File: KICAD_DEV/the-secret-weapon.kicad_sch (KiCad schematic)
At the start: 0 parts

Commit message: ground pour + core SoC STM32H757
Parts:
- added U1: STM32H7A3IGTx, Package_QFP:LQFP-176_24x24mm_P0.5mm, symbol MCU_ST_STM32H7:STM32H7A3IGTx
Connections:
- new net GND: U1.102 (VSS), U1.113 (VSS), U1.126 (VSS), U1.135 (VSS), U1.14 (VSS), U1.148 (VSS), U1.158 (VSS), U1.22 (VSS), U1.37 (VSSA), U1.48 (VSS), U1.61 (VSS), U1.71 (VSS), U1.90 (VSS)

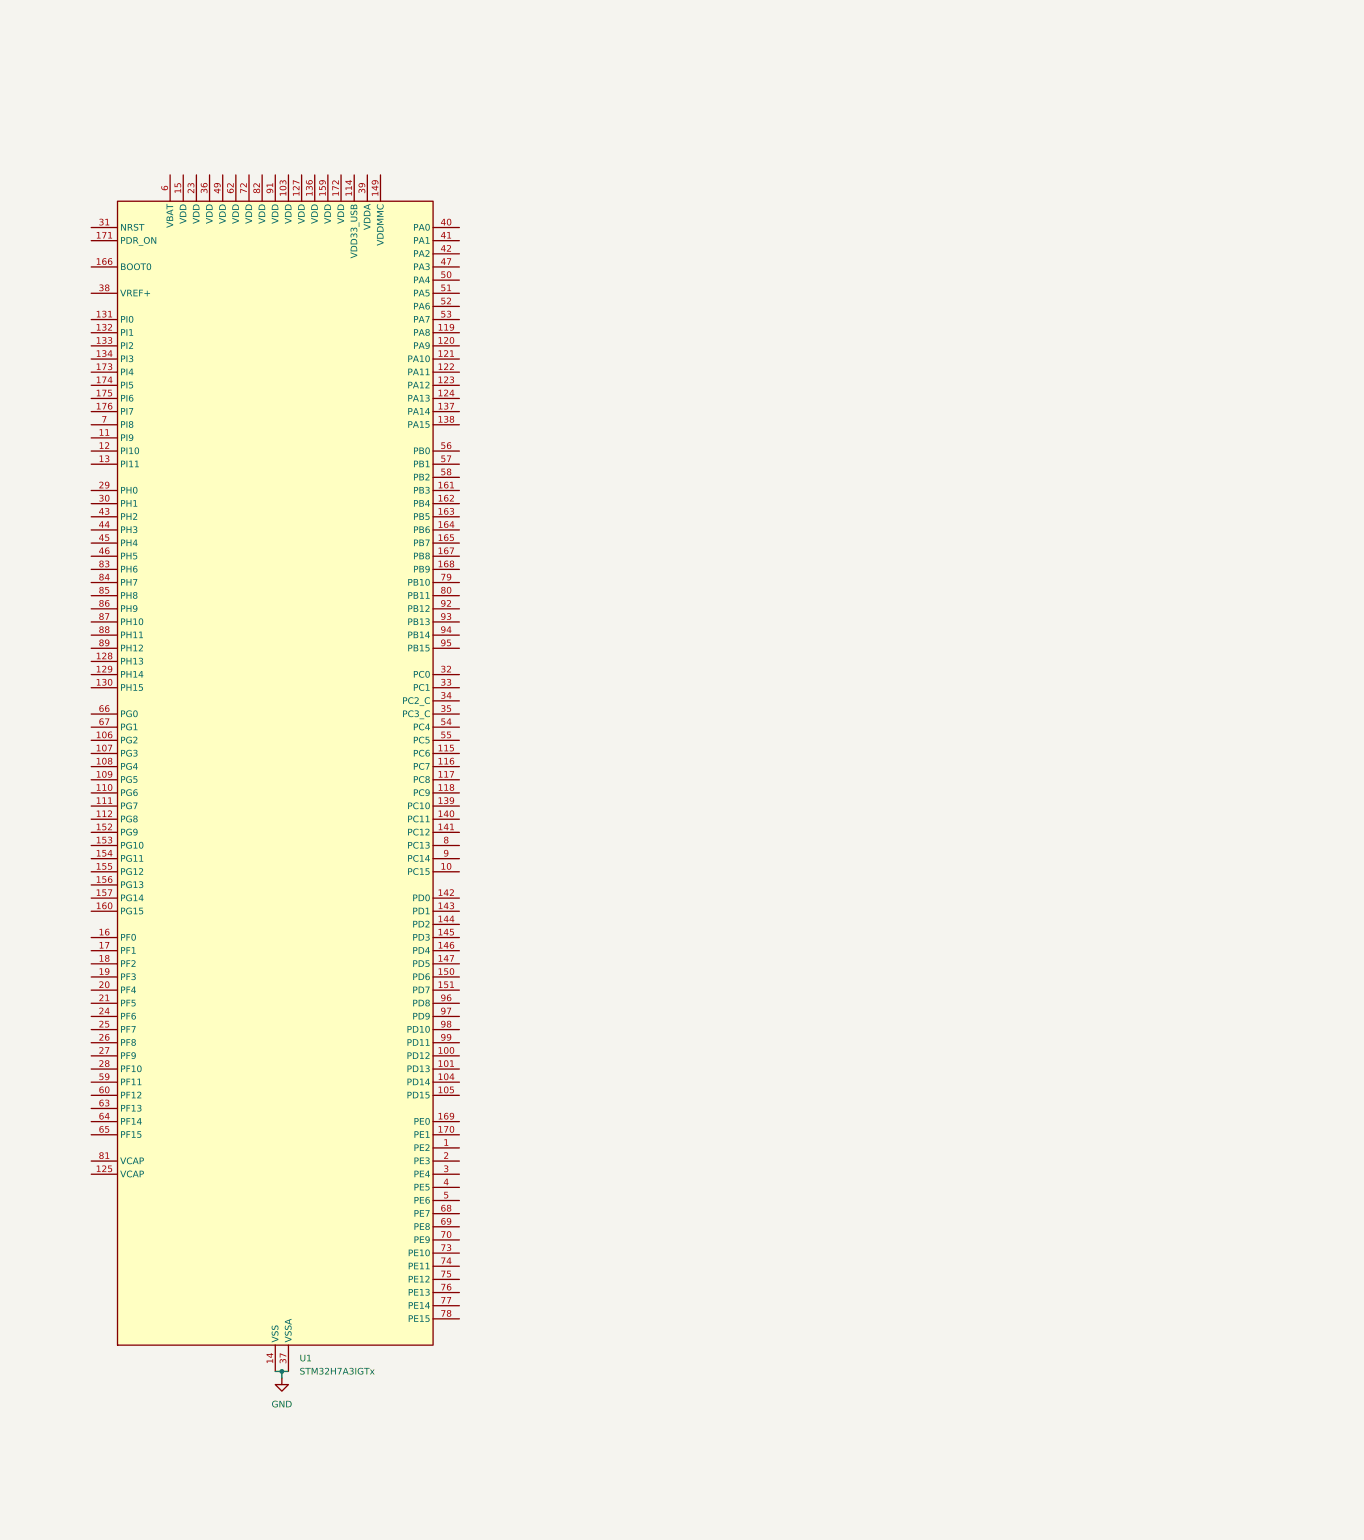
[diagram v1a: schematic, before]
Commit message: accidently used the wrong symbol
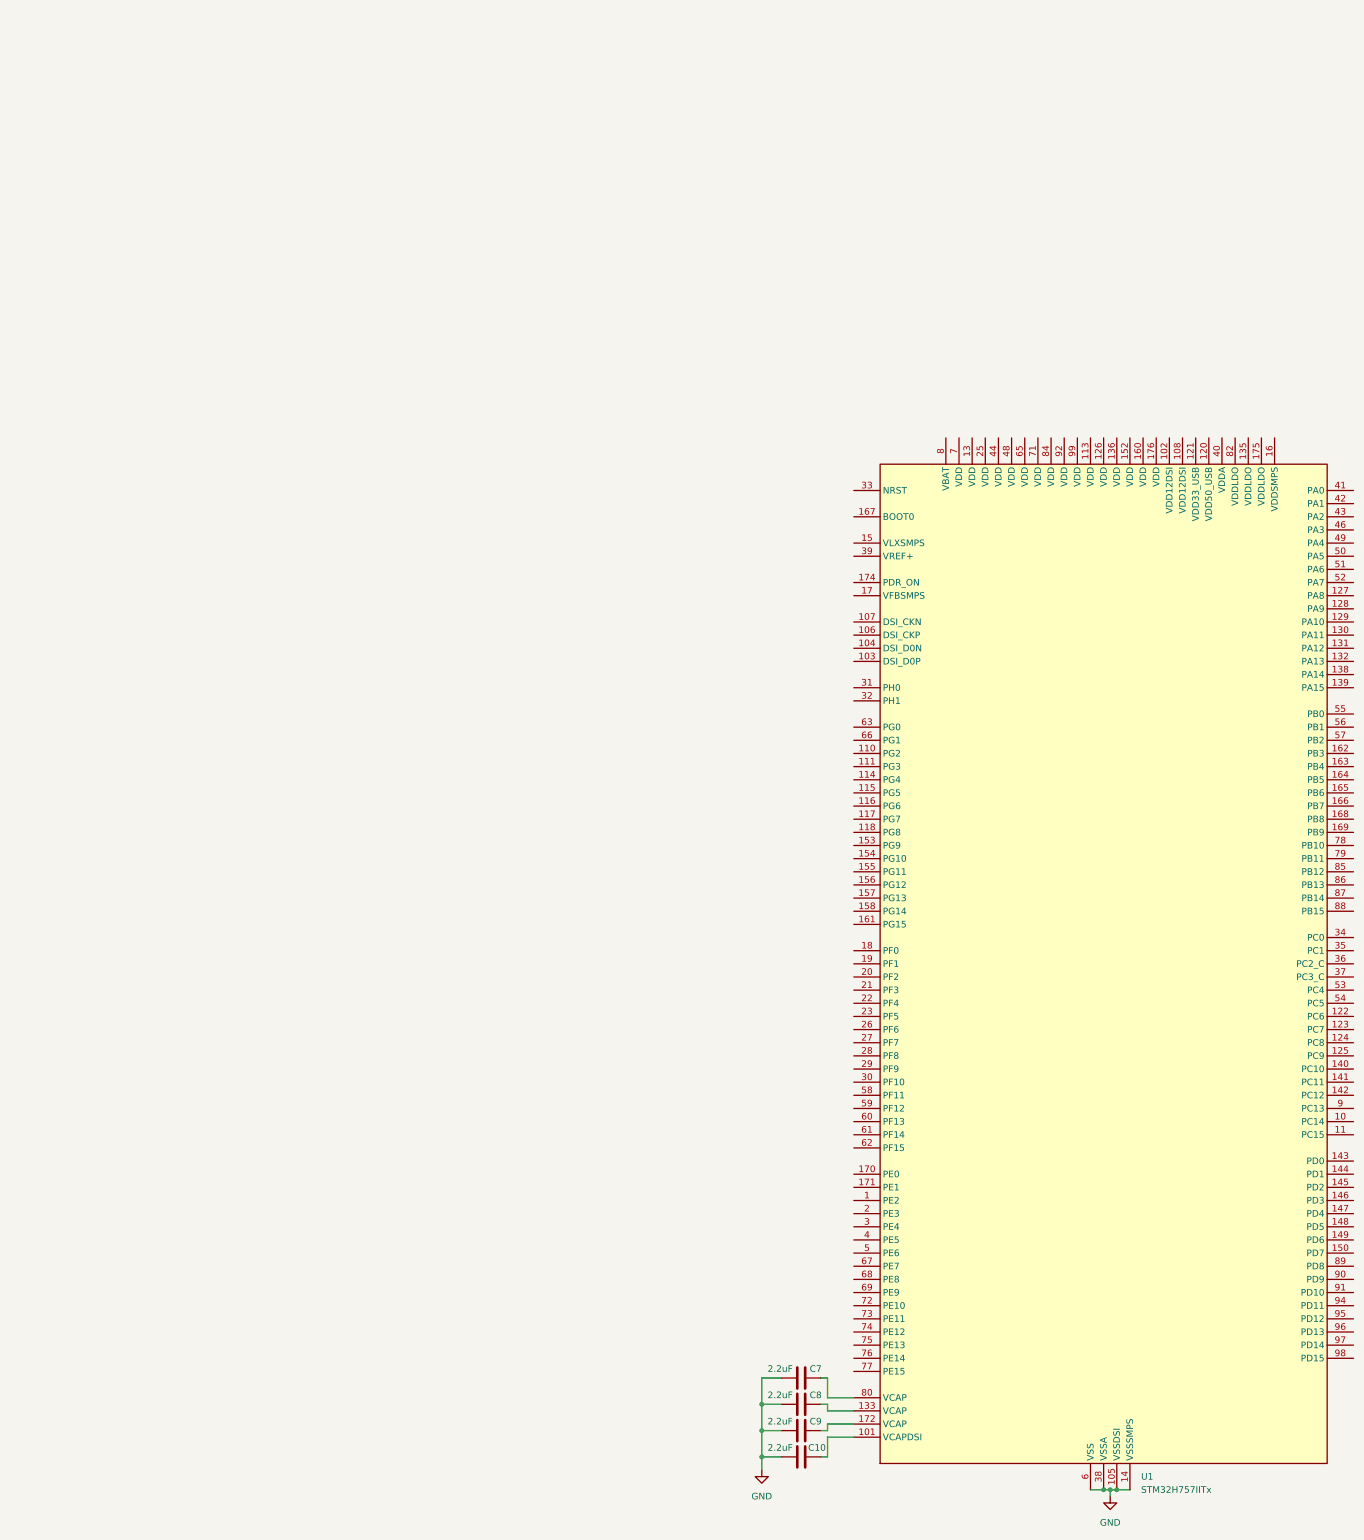
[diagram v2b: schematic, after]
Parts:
- removed U1: STM32H7A3IGTx, Package_QFP:LQFP-176_24x24mm_P0.5mm, symbol MCU_ST_STM32H7:STM32H7A3IGTx
- added C10, C7, C8, C9: 2.2uF, symbol Device:C
- added U1: STM32H757IITx, Package_QFP:LQFP-176_24x24mm_P0.5mm, symbol MCU_ST_STM32H7:STM32H757IITx
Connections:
- net GND: now also C10.1, C7.1, C8.1, C9.1, U1.100 (VSS), U1.105 (VSSDSI), U1.109 (VSSDSI), U1.112 (VSS), U1.119 (VSS), U1.12 (VSS), U1.134 (VSS), U1.137 (VSS), U1.14 (VSSSMPS), U1.151 (VSS), U1.159 (VSS), U1.173 (VSS), U1.24 (VSS), U1.38 (VSSA), U1.45 (VSS), U1.47 (VSS), U1.6 (VSS), U1.64 (VSS), U1.70 (VSS), U1.81 (VSS), U1.83 (VSS), U1.93 (VSS)
- new net: C9.2, U1.172 (VCAP)
- new net: C10.2, U1.101 (VCAPDSI)
- new net: C8.2, U1.133 (VCAP)
- new net: C7.2, U1.80 (VCAP)

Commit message: working on USB PD
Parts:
- added J1: USB_C_Receptacle_USB2.0_14P, symbol Connector:USB_C_Receptacle_USB2.0_14P
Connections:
- net GND: now also J1.A1 (GND), J1.A12 (GND), J1.B1 (GND), J1.B12 (GND), J1.S1 (SHIELD)
- net +1V2: now reaches U1.102 (VDD12DSI)
- net +1V2: now also U1.108 (VDD12DSI)
- net +3V3: now reaches U1.113 (VDD)
- net +3V3: now also U1.126 (VDD), U1.13 (VDD), U1.136 (VDD), U1.152 (VDD), U1.160 (VDD), U1.176 (VDD), U1.25 (VDD), U1.44 (VDD), U1.48 (VDD), U1.65 (VDD), U1.7 (VDD), U1.71 (VDD), U1.84 (VDD), U1.92 (VDD), U1.99 (VDD)
- new net: J1.A4 (VBUS), J1.A9 (VBUS), J1.B4 (VBUS), J1.B9 (VBUS)
- new net: J1.A6 (D+), J1.B6 (D+)
- new net: J1.A7 (D-), J1.B7 (D-)
- no-connect marks 0 -> 1

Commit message: adding my custom USB PD symbol
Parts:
- added U2: TPS26750, Package_DFN_QFN:Texas_RSN_WQFN-32-1EP_4x4mm_P0.4mm_EP2.8x2.8mm_ThermalVias, symbol kai-library:TPS26750
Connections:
- new net: U2.11 (GND), U2.12 (GND), U2.14 (GND), U2.16 (I2Cc_SCL), U2.17 (~{I2Cc_IRQ}), U2.31 (GND), U2.34 (GND), U2.39 (GND)
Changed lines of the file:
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@@
+	)
+	(symbol
+		(lib_id "kai-library:TPS26750")
+		(at 168.91 63.5 0)
+		(unit 1)
+		(exclude_from_sim no)
+		(in_bom yes)
+		(on_board yes)
+		(dnp no)
+		(fields_autoplaced yes)
+		(property "Reference" "U2"
+			(at 168.91 40.64 0)
+			(effects
+				(font
+					(size 1.27 1.27)
+				)
+			)
+		)
+		(property "Value" "TPS26750"
+			(at 168.91 43.18 0)
+			(effects
+				(font
+					(size 1.27 1.27)
+				)
+			)
+		)
+		(property "Footprint" "Package_DFN_QFN:Texas_RSN_WQFN-32-1EP_4x4mm_P0.4mm_EP2.8x2.8mm_ThermalVias"
+			(at 168.91 63.5 0)
+			(effects
+				(font
+					(size 1.27 1.27)
+				)
+				(hide yes)
+			)
+		)
+		(property "Datasheet" "https://www.ti.com/lit/ds/symlink/tps26750.pdf?ts=1761278028610&ref_url=https%253A%252F%252Fwww.ti.com%252Fproduct%252FTPS26750"
+			(at 168.91 63.5 0)
+			(effects
+				(font
+					(size 1.27 1.27)
+				)
+				(hide yes)
+			)
+		)
+		(property "Description" "TPS26750 USB Type-C® and USB PD Controller With Integrated Power Switches Optimized for Power Applications"
+			(at 168.91 63.5 0)
+			(effects
+				(font
+					(size 1.27 1.27)
+				)
+				(hide yes)
+			)
+		)
+		(pin "6"
+		)
+		(pin "5"
+		)
+		(pin "13"
+		)
+		(pin "12"
+		)
+		(pin "25"
+		)
+		(pin "24"
+		)
+		(pin "1"
+		)
+		(pin "18"
+		)
+		(pin "14"
+		)
+		(pin "10"
+		)
+		(pin "34"
+		)
+		(pin "26"
+		)
+		(pin "16"
+		)
+		(pin "17"
+		)
+		(pin "9"
+		)
+		(pin "16"
+		)
+		(pin "15"
+		)
+		(pin "8"
+		)
+		(pin "28"
+		)
+		(pin "39"
+		)
+		(pin "11"
+		)
+		(pin "22"
+		)
+		(pin "17"
+		)
+		(pin "30"
+		)
+		(pin "23"
+		)
+		(pin "19"
+		)
+		(pin "7"
+		)
+		(pin "32"
+		)
+		(pin "31"
+		)
+		(pin "2"
+		)
+		(pin "20"
+		)
+		(pin "4"
+		)
+		(pin "31"
+		)
+		(pin "3"
+		)
+		(instances
+			(project ""
+				(path "/28389848-e686-45d1-8788-e912d76b51d3"
+					(reference "U2")
+					(unit 1)
+				)
+			)
+		)
 	)
 	(symbol

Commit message: revising my USB PD
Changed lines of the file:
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@@
+	)
+	(symbol
+		(lib_id "kai-library:TPS26750")
+		(at 166.37 66.04 0)
+		(unit 1)
+		(exclude_from_sim no)
+		(in_bom yes)
+		(on_board yes)
+		(dnp no)
+		(fields_autoplaced yes)
+		(property "Reference" "U2"
+			(at 166.37 43.18 0)
+			(effects
+				(font
+					(size 1.27 1.27)
+				)
+			)
+		)
+		(property "Value" "TPS26750"
+			(at 166.37 45.72 0)
+			(effects
+				(font
+					(size 1.27 1.27)
+				)
+			)
+		)
+		(property "Footprint" "Package_DFN_QFN:Texas_RSN_WQFN-32-1EP_4x4mm_P0.4mm_EP2.8x2.8mm_ThermalVias"
+			(at 166.37 66.04 0)
+			(effects
+				(font
+					(size 1.27 1.27)
+				)
+				(hide yes)
+			)
+		)
+		(property "Datasheet" "https://www.ti.com/lit/ds/symlink/tps26750.pdf?ts=1761278028610&ref_url=https%253A%252F%252Fwww.ti.com%252Fproduct%252FTPS26750"
+			(at 166.37 66.04 0)
+			(effects
+				(font
+					(size 1.27 1.27)
+				)
+				(hide yes)
+			)
+		)
+		(property "Description" "TPS26750 USB Type-C® and USB PD Controller With Integrated Power Switches Optimized for Power Applications"
+			(at 166.37 66.04 0)
+			(effects
+				(font
+					(size 1.27 1.27)
+				)
+				(hide yes)
+			)
+		)
+		(pin "30"
+		)
+		(pin "31"
+		)
+		(pin "12"
+		)
+		(pin "34"
+		)
+		(pin "3"
+		)
+		(pin "20"
+		)
+		(pin "22"
+		)
+		(pin "10"
+		)
+		(pin "16"
+		)
+		(pin "31"
+		)
+		(pin "13"
+		)
+		(pin "39"
+		)
+		(pin "9"
+		)
+		(pin "16"
+		)
+		(pin "23"
+		)
+		(pin "1"
+		)
+		(pin "17"
+		)
+		(pin "2"
+		)
+		(pin "14"
+		)
+		(pin "7"
+		)
+		(pin "15"
+		)
+		(pin "5"
+		)
+		(pin "11"
+		)
+		(pin "8"
+		)
+		(pin "32"
+		)
+		(pin "26"
+		)
+		(pin "18"
+		)
+		(pin "6"
+		)
+		(pin "24"
+		)
+		(pin "25"
+		)
+		(pin "4"
+		)
+		(pin "17"
+		)
+		(pin "28"
+		)
+		(instances
+			(project ""
+				(path "/28389848-e686-45d1-8788-e912d76b51d3"
+					(reference "U2")
+					(unit 1)
+				)
+			)
+		)
 	)
 	(symbol
@@
 					(unit 1)
 				)
-			)
-		)
-	)
-	(symbol
-		(lib_id "kai-library:TPS26750")
-		(at 168.91 63.5 0)
-		(unit 1)
-		(exclude_from_sim no)
-		(in_bom yes)
-		(on_board yes)
-		(dnp no)
-		(fields_autoplaced yes)
-		(property "Reference" "U2"
-			(at 168.91 40.64 0)
-			(effects
-				(font
-					(size 1.27 1.27)
-				)
-			)
-		)
-		(property "Value" "TPS26750"
-			(at 168.91 43.18 0)
-			(effects
-				(font
-					(size 1.27 1.27)
-				)
-			)
-		)
-		(property "Footprint" "Package_DFN_QFN:Texas_RSN_WQFN-32-1EP_4x4mm_P0.4mm_EP2.8x2.8mm_ThermalVias"
-			(at 168.91 63.5 0)
-			(effects
-				(font
-					(size 1.27 1.27)
-				)
-				(hide yes)
-			)
-		)
-		(property "Datasheet" "https://www.ti.com/lit/ds/symlink/tps26750.pdf?ts=1761278028610&ref_url=https%253A%252F%252Fwww.ti.com%252Fproduct%252FTPS26750"
-			(at 168.91 63.5 0)
-			(effects
-				(font
-					(size 1.27 1.27)
-				)
-				(hide yes)
-			)
-		)
-		(property "Description" "TPS26750 USB Type-C® and USB PD Controller With Integrated Power Switches Optimized for Power Applications"
-			(at 168.91 63.5 0)
-			(effects
-				(font
-					(size 1.27 1.27)
-				)
-				(hide yes)
-			)
-		)
-		(pin "6"
-		)
-		(pin "5"
-		)
-		(pin "13"
-		)
-		(pin "12"
-		)
-		(pin "25"
-		)
-		(pin "24"
-		)
-		(pin "1"
-		)
-		(pin "18"
-		)
-		(pin "14"
-		)
-		(pin "10"
-		)
-		(pin "34"
-		)
-		(pin "26"
-		)
-		(pin "16"
-		)
-		(pin "17"
-		)
-		(pin "9"
-		)
-		(pin "16"
-		)
-		(pin "15"
-		)
-		(pin "8"
-		)
-		(pin "28"
-		)
-		(pin "39"
-		)
-		(pin "11"
-		)
-		(pin "22"
-		)
-		(pin "17"
-		)
-		(pin "30"
-		)
-		(pin "23"
-		)
-		(pin "19"
-		)
-		(pin "7"
-		)
-		(pin "32"
-		)
-		(pin "31"
-		)
-		(pin "2"
-		)
-		(pin "20"
-		)
-		(pin "4"
-		)
-		(pin "31"
-		)
-		(pin "3"
-		)
-		(instances
-			(project ""
-				(path "/28389848-e686-45d1-8788-e912d76b51d3"
-					(reference "U2")
-					(unit 1)
-				)

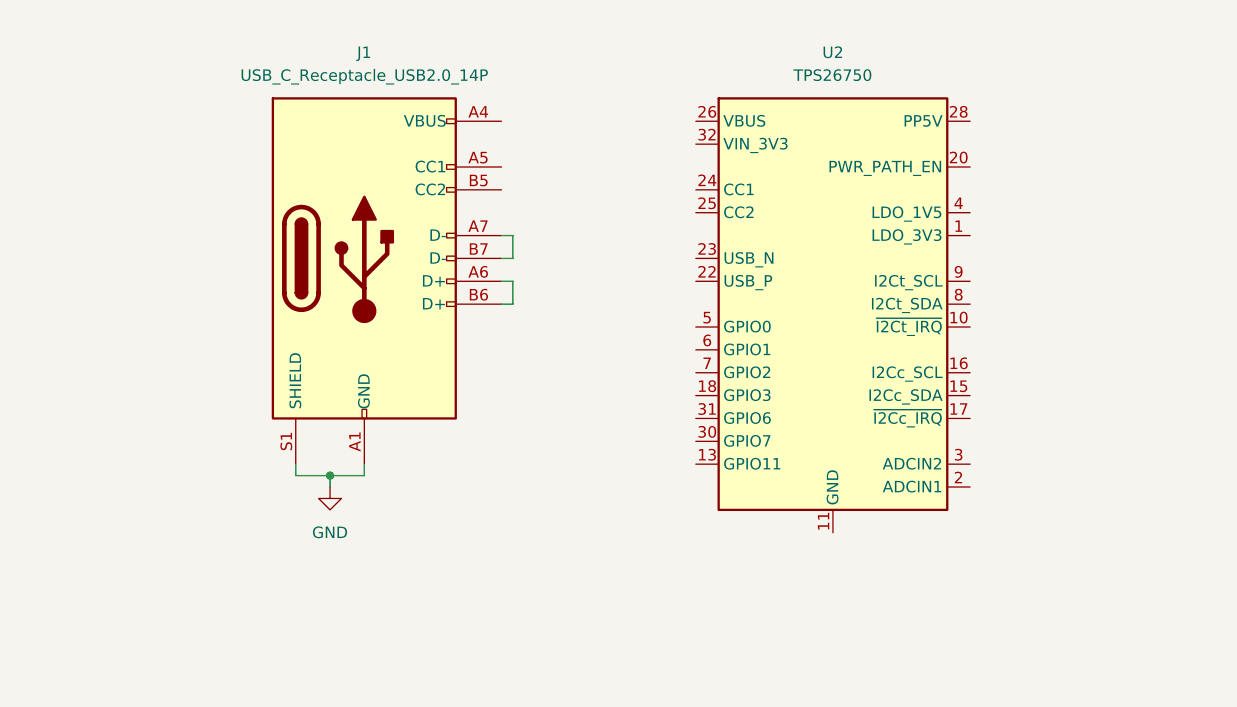
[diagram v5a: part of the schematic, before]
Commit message: wiring USB-C
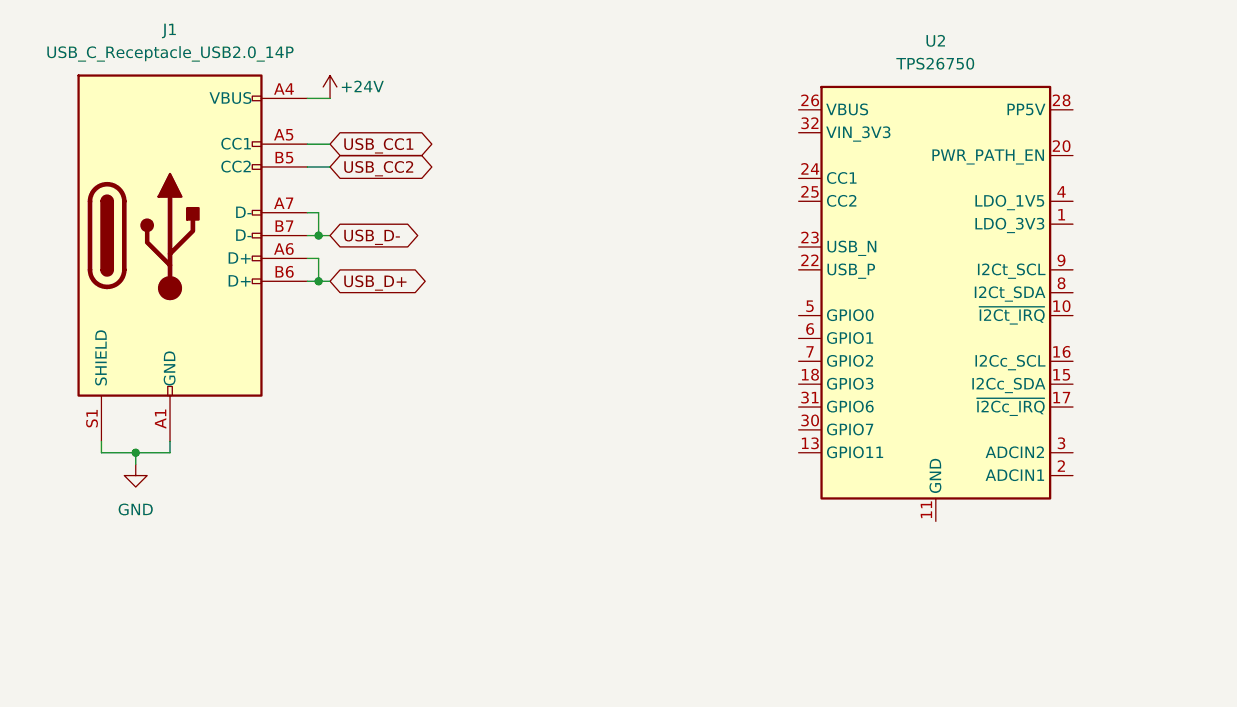
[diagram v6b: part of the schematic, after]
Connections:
- net +24V: now reaches J1.A4 (VBUS), J1.A9 (VBUS), J1.B4 (VBUS), J1.B9 (VBUS)
- net USB_CC1: now reaches J1.A5 (CC1)
- net USB_D+: now reaches J1.A6 (D+), J1.B6 (D+)
- net USB_D-: now reaches J1.A7 (D-), J1.B7 (D-)
- net USB_CC2: now reaches J1.B5 (CC2)
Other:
- moved on the sheet: J1, U2
